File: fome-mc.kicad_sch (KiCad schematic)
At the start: 3 parts, among them J1 TE_776163-1, J2 TE_776163-2

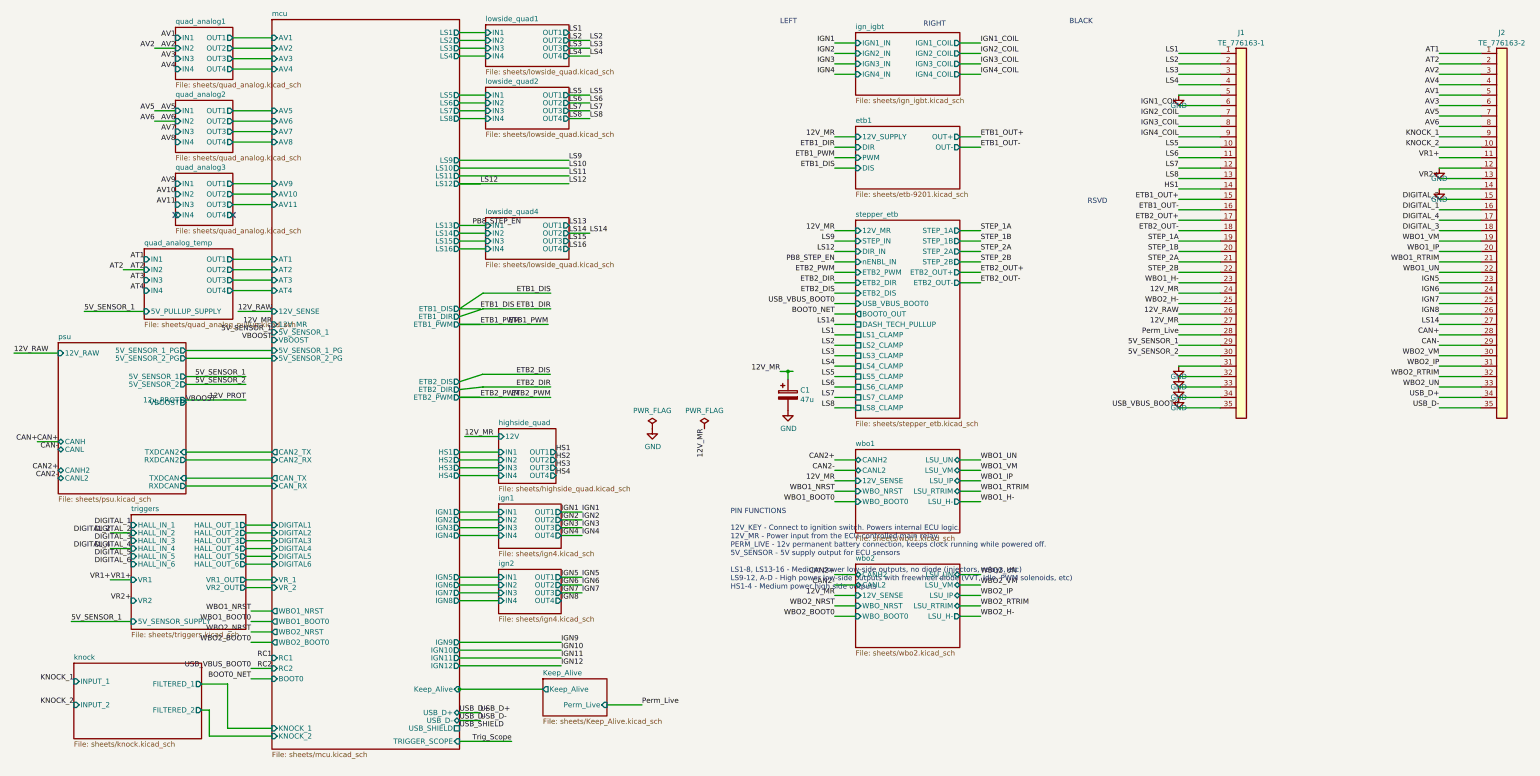
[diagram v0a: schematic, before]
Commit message: Remediate power supply, main relay keep-alive, and schematic ERC to 0 errors
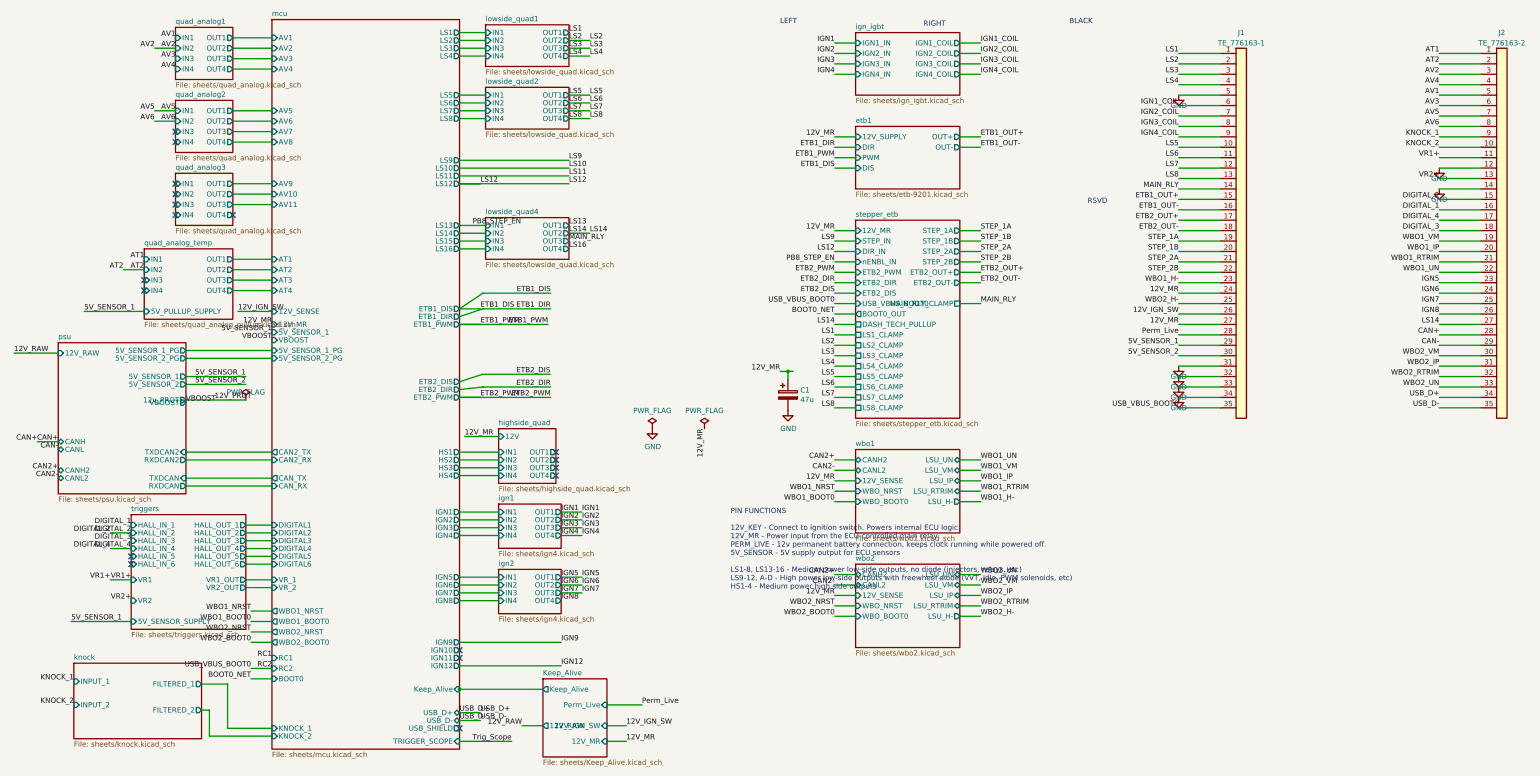
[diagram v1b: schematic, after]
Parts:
- C1: PN EEH-AZF1H560B -> EEHZC1H470P
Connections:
- net 12V_RAW: no longer J1.26 (Pin_26)
- net HS1 renamed MAIN_RLY
- new net 12V_IGN_SW: J1.26 (Pin_26)
- no-connect marks 2 -> 18
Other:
- sheet Keep_Alive ports: added 12V_IGN_SW, 12V_MR, 12V_RAW; removed none
- sheet stepper_etb ports: added MAIN_RLY_CLAMP; removed none

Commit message: Re-integrate ATWINC1500-MR210UB Wi-Fi on SPI4 and remap WBO1/2 reset/boot pins (FOMEMC-2)
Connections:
- no-connect marks 18 -> 16
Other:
- sheet mcu ports: added none; removed IGN10, IGN11, IGN12, IGN9
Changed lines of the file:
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@@
 	(wire
 		(pts
-			(xy 114.3 168.91) (xy 139.065 168.91)
-		)
-		(stroke
-			(width 0)
-			(type default)
-		)
-	)
-	(wire
-		(pts
 			(xy 194.31 102.87) (xy 195.58 102.87)
 		)
@@
 	(wire
 		(pts
-			(xy 114.3 174.625) (xy 139.065 174.625)
-		)
-		(stroke
-			(width 0)
-			(type default)
-		)
-	)
-	(wire
-		(pts
 			(xy 120.65 73.025) (xy 114.3 73.025)
 		)
@@
 		)
 	)
-	(label "IGN9"
-		(at 139.065 168.91 0)
-		(fields_autoplaced yes)
-		(effects
-			(font
-				(size 1.27 1.27)
-			)
-			(justify left bottom)
-		)
-	)
 	(label "LS12"
 		(at 140.97 57.15 0)
@@
 		)
 	)
-	(label "IGN12"
-		(at 139.065 174.625 0)
-		(fields_autoplaced yes)
-		(effects
-			(font
-				(size 1.27 1.27)
-			)
-			(justify left bottom)
-		)
-	)
 	(label "5V_SENSOR_1"
 		(at 22.86 88.265 0)
@@
 			)
 		)
-		(pin "IGN9" output
-			(at 114.3 168.91 0)
-			(effects
-				(font
-					(size 1.27 1.27)
-				)
-				(justify right)
-			)
-		)
-		(pin "IGN10" output
-			(at 114.3 170.815 0)
-			(effects
-				(font
-					(size 1.27 1.27)
-				)
-				(justify right)
-			)
-		)
-		(pin "IGN11" output
-			(at 114.3 172.72 0)
-			(effects
-				(font
-					(size 1.27 1.27)
-				)
-				(justify right)
-			)
-		)
-		(pin "IGN12" output
-			(at 114.3 174.625 0)
-			(effects
-				(font
-					(size 1.27 1.27)
-				)
-				(justify right)
-			)
-		)
 		(pin "USB_D-" bidirectional
 			(at 114.3 187.96 0)
@@
 		(at 137.795 128.27)
 	)
-	(no_connect
-		(at 114.3 170.815)
-	)
-	(no_connect
-		(at 114.3 172.72)
-	)
 )

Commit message: Add MAX9924UAUB+ (U13/U14) differential VR conditioners and switch Hall Schmitt triggers (U8/U9/U10) to +3V3 (FOMEMC-6)
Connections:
- net GND: no longer J2.12 (Pin_12), J2.14 (Pin_14)
- new net VR1-: J2.12 (Pin_12)
- new net VR2-: J2.14 (Pin_14)
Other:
- sheet triggers ports: added VR1-, VR2-; removed none
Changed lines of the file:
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@@
 		)
 	)
-	(label "VR1+"
-		(at 34.29 153.67 180)
+	(label "VR1-"
+		(at 34.29 156.21 180)
+		(fields_autoplaced yes)
+		(effects
+			(font
+				(size 1.27 1.27)
+			)
+			(justify right bottom)
+		)
+	)
+	(label "VR2-"
+		(at 34.29 161.29 180)
 		(fields_autoplaced yes)
 		(effects
@@
 			)
 		)
+		(pin "VR1-" input
+			(at 34.29 156.21 180)
+			(effects
+				(font
+					(size 1.27 1.27)
+				)
+				(justify left)
+			)
+		)
+		(pin "VR2-" input
+			(at 34.29 161.29 180)
+			(effects
+				(font
+					(size 1.27 1.27)
+				)
+				(justify left)
+			)
+		)
 		(pin "VR1_OUT" output
 			(at 62.23 153.67 0)
@@
 		)
 	)
-	(symbol
-		(lib_id "power:GND")
-		(at 353.06 53.34 0)
-		(unit 1)
-		(exclude_from_sim no)
-		(in_bom yes)
-		(on_board yes)
-		(dnp no)
-		(property "Reference" "#PWR07212" (at 353.06 55.88 0) (effects (font (size 1.27 1.27)) (hide yes)))
-		(property "Value" "GND" (at 353.06 55.88 0) (effects (font (size 1.27 1.27))))
-		(property "Footprint" "" (at 353.06 53.34 0) (effects (font (size 1.27 1.27)) (hide yes)))
-		(property "Datasheet" "" (at 353.06 53.34 0) (effects (font (size 1.27 1.27)) (hide yes)))
-		(pin "1")
-		(instances
-			(project "fome-mc" (path "/3b9c5ffd-e59b-402d-8c5e-052f7ca643a4" (reference "#PWR07212") (unit 1)))
-			(project "fome-mc" (path "/3b9c5ffd-e59b-402d-8c5e-052f7ca643a4" (reference "#PWR07212") (unit 1)))
+	(label "VR1-"
+		(at 353.06 53.34 180)
+		(fields_autoplaced yes)
+		(effects
+			(font
+				(size 1.27 1.27)
+			)
+			(justify right bottom)
 		)
 	)
@@
 		)
 	)
-	(symbol
-		(lib_id "power:GND")
-		(at 353.06 58.42 0)
-		(unit 1)
-		(exclude_from_sim no)
-		(in_bom yes)
-		(on_board yes)
-		(dnp no)
-		(property "Reference" "#PWR07214" (at 353.06 60.96 0) (effects (font (size 1.27 1.27)) (hide yes)))
-		(property "Value" "GND" (at 353.06 60.96 0) (effects (font (size 1.27 1.27))))
-		(property "Footprint" "" (at 353.06 58.42 0) (effects (font (size 1.27 1.27)) (hide yes)))
-		(property "Datasheet" "" (at 353.06 58.42 0) (effects (font (size 1.27 1.27)) (hide yes)))
-		(pin "1")
-		(instances
-			(project "fome-mc" (path "/3b9c5ffd-e59b-402d-8c5e-052f7ca643a4" (reference "#PWR07214") (unit 1)))
-			(project "fome-mc" (path "/3b9c5ffd-e59b-402d-8c5e-052f7ca643a4" (reference "#PWR07214") (unit 1)))
+	(label "VR2-"
+		(at 353.06 58.42 180)
+		(fields_autoplaced yes)
+		(effects
+			(font
+				(size 1.27 1.27)
+			)
+			(justify right bottom)
 		)
 	)

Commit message: Add D210 BZT52C6V8 BOOT0 threshold Zener, R217/R218/D211 PA9 VBUS sense divider/clamp, and SMCJ24A TVS protection on 12V_RAW and 12V_MR (FOMEMC-7)
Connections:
- net RC2: no longer J1.35 (Pin_35)
- new net USB_VBUS_BOOT0: J1.35 (Pin_35)
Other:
- sheet stepper_etb ports: added VBUS_SENSE_OUT; removed none
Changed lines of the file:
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@@
 			(effects (font (size 1.27 1.27)) (justify right))
 		)
+		(pin "VBUS_SENSE_OUT" output
+			(at 236.22 88.9 0)
+			(effects (font (size 1.27 1.27)) (justify right))
+		)
 		(instances
-			(project "fome-mc" (path "/3b9c5ffd-e59b-402d-8c5e-052f7ca643a4" (page "19")))
 			(project "fome-mc" (path "/3b9c5ffd-e59b-402d-8c5e-052f7ca643a4" (page "19")))
 		)
@@
 	(wire
 		(pts
-			(xy 63.5 175.26) (xy 68.58 175.26)
-		)
-		(stroke
-			(width 0)
-			(type default)
-		)
-	)
-	(label "USB_VBUS_BOOT0"
-		(at 63.5 175.26 180)
-		(fields_autoplaced yes)
-		(effects
-			(font
-				(size 1.27 1.27)
-			)
-			(justify right bottom)
-		)
-	)
+			(xy 236.22 88.9) (xy 241.3 88.9)
+		)
+		(stroke
+			(width 0)
+			(type default)
+		)
+	)
+	(label "RC2"
+		(at 241.3 88.9 0)
+		(fields_autoplaced yes)
+		(effects
+			(font
+				(size 1.27 1.27)
+			)
+			(justify left bottom)
+		)
+	)

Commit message: Complete FOMEMC-11, FOMEMC-12, and FOMEMC-16: sync 492 PCB footprints, restore min_resolved_spokes=2 (0 starved thermals), enable teardrops, enforce >=1.2mm IGBT collector clearance, widen /IGN1..4_COIL, add WBO heater copper zones, and refresh CPL/BOM/renders
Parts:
- added R219: 1.5k, Resistor_SMD:R_0603_1608Metric, symbol Device:R
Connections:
- net 5V_SENSOR_1: now also R219.1
- net AV6: now also R219.2
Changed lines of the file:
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@@
 		(color 0 0 0 0)
 	)
-	(junction
-		(at 114.3 180.34)
-		(diameter 0)
-		(color 0 0 0 0)
-	)
 	(no_connect
 		(at 45.085 64.77)
@@
 	(wire
 		(pts
-			(xy 194.31 102.87) (xy 195.58 102.87)
-		)
-		(stroke
-			(width 0)
-			(type default)
-		)
-	)
-	(wire
-		(pts
 			(xy 62.23 106.045) (xy 47.625 106.045)
 		)
@@
 	(wire
 		(pts
-			(xy 114.3 180.325) (xy 114.3 180.34)
-		)
-		(stroke
-			(width 0)
-			(type default)
-		)
-	)
-	(wire
-		(pts
 			(xy 120.65 41.275) (xy 114.3 41.275)
 		)
@@
 		)
 	)
-	(wire
-		(pts
-			(xy 194.31 102.87) (xy 194.343 102.899)
-		)
-		(stroke
-			(width 0)
-			(type default)
-		)
-	)
 	(text "LEFT"
 		(exclude_from_sim no)
@@
 	(wire
 		(pts
-			(xy 114.3 87.63) (xy 119.38 87.63)
-		)
-		(stroke
-			(width 0)
-			(type default)
-		)
-	)
-	(label "ETB1_DIS"
-		(at 119.38 87.63 0)
-		(fields_autoplaced yes)
-		(effects
-			(font
-				(size 1.27 1.27)
-			)
-			(justify left bottom)
-		)
-	)
-	(wire
-		(pts
 			(xy 114.3 91.44) (xy 119.38 91.44)
 		)
@@
 		)
 	)
-	(label "LS14"
+	(label "LS8"
 		(at 205.74 91.44 180)
 		(fields_autoplaced yes)
@@
 		(at 137.795 128.27)
 	)
+	(wire
+		(pts
+			(xy 19.05 41.91) (xy 21.59 41.91)
+		)
+		(stroke (width 0) (type default))
+	)
+	(label "5V_SENSOR_1"
+		(at 19.05 41.91 180)
+		(fields_autoplaced yes)
+		(effects (font (size 1.27 1.27)) (justify right bottom))
+	)
+	(wire
+		(pts
+			(xy 29.21 41.91) (xy 34.29 41.91)
+		)
+		(stroke (width 0) (type default))
+	)
+	(label "AV6"
+		(at 34.29 41.91 0)
+		(fields_autoplaced yes)
+		(effects (font (size 1.27 1.27)) (justify left bottom))
+	)
+	(symbol
+		(lib_id "Device:R")
+		(at 25.4 41.91 90)
+		(unit 1)
+		(exclude_from_sim no)
+		(in_bom yes)
+		(on_board yes)
+		(dnp no)
+		(fields_autoplaced yes)
+		(property "Reference" "R219"
+			(at 25.4 39.37 0)
+			(effects (font (size 1.27 1.27)))
+		)
+		(property "Value" "1.5k"
+			(at 25.4 44.45 0)
+			(effects (font (size 1.27 1.27)))
+		)
+		(property "Footprint" "Resistor_SMD:R_0603_1608Metric"
+			(at 25.4 41.91 0)
+			(effects (font (size 1.27 1.27)) (hide yes))
+		)
+		(property "Datasheet" "~"
+			(at 25.4 41.91 0)
+			(effects (font (size 1.27 1.27)) (hide yes))
+		)
+		(property "Description" "1.5kOhm 1% 0603 Thick Film Resistor (Gear Position Pull-Up)"
+			(at 25.4 41.91 0)
+			(effects (font (size 1.27 1.27)) (hide yes))
+		)
+		(property "PN" "0603WAF1501T5E"
+			(at 25.4 41.91 0)
+			(effects (font (size 1.27 1.27)) (hide yes))
+		)
+		(property "LCSC" "C22843"
+			(at 25.4 41.91 0)
+			(effects (font (size 1.27 1.27)) (hide yes))
+		)
+		(pin "1")
+		(pin "2")
+		(instances
+			(project "fome-mc"
+				(path "/3b9c5ffd-e59b-402d-8c5e-052f7ca643a4"
+					(reference "R219")
+					(unit 1)
+				)
+			)
+		)
+	)
 )

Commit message: Remediate FOMEMC-17..20: 50V X7R PSU caps & 42V INJ clamp DNP, U29 DS70005304F footprint + 1P3V bypass, HV_IGN 0.50mm clearance + U25 decoupling, and 0 ERC violations
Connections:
- no-connect marks 16 -> 18
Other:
- sheet mcu ports: added none; removed LS10, LS11, RC1, TRIGGER_SCOPE
- sheet psu ports: added 12V_PROT; removed 12v_PROT
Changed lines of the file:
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@@
 	(wire
 		(pts
-			(xy 114.3 53.34) (xy 140.97 53.34)
-		)
-		(stroke
-			(width 0)
-			(type default)
-		)
-	)
-	(wire
-		(pts
 			(xy 120.015 106.68) (xy 114.3 107.315)
 		)
@@
 	(wire
 		(pts
-			(xy 114.3 55.245) (xy 140.97 55.245)
-		)
-		(stroke
-			(width 0)
-			(type default)
-		)
-	)
-	(wire
-		(pts
 			(xy 68.58 130.81) (xy 47.625 130.81)
 		)
@@
 	(wire
 		(pts
-			(xy 114.3 193.04) (xy 127 193.04)
-		)
-		(stroke
-			(width 0)
-			(type default)
-		)
-	)
-	(wire
-		(pts
 			(xy 114.3 139.065) (xy 123.825 139.065)
 		)
@@
 		)
 	)
-	(label "LS16"
-		(at 140.97 73.025 0)
-		(fields_autoplaced yes)
-		(effects
-			(font
-				(size 1.27 1.27)
-			)
-			(justify left bottom)
-		)
-	)
 	(label "12V_RAW"
 		(at 5.715 98.425 0)
@@
 		)
 	)
-	(label "Trig_Scope"
-		(at 127 193.04 180)
-		(fields_autoplaced yes)
-		(effects
-			(font
-				(size 1.27 1.27)
-			)
-			(justify right bottom)
-		)
-	)
 	(label "LS1"
 		(at 140.97 20.32 0)
@@
 		)
 	)
-	(label "LS10"
-		(at 140.97 53.34 0)
-		(fields_autoplaced yes)
-		(effects
-			(font
-				(size 1.27 1.27)
-			)
-			(justify left bottom)
-		)
-	)
 	(label "CAN-"
 		(at 16.51 121.92 180)
@@
 		)
 	)
-	(label "RC1"
-		(at 68.58 172.72 180)
-		(fields_autoplaced yes)
-		(effects
-			(font
-				(size 1.27 1.27)
-			)
-			(justify right bottom)
-		)
-	)
 	(label "LS9"
 		(at 140.97 51.435 0)
@@
 		)
 	)
-	(label "LS13"
-		(at 140.97 67.31 0)
-		(fields_autoplaced yes)
-		(effects
-			(font
-				(size 1.27 1.27)
-			)
-			(justify left bottom)
-		)
-	)
 	(label "IGN4"
 		(at 139.065 142.875 0)
@@
 		)
 	)
-	(label "LS11"
-		(at 140.97 55.245 0)
-		(fields_autoplaced yes)
-		(effects
-			(font
-				(size 1.27 1.27)
-			)
-			(justify left bottom)
-		)
-	)
 	(label "KNOCK_1"
 		(at 20.32 178.435 180)
@@
 			)
 		)
-		(pin "LS10" output
-			(at 114.3 53.34 0)
-			(effects
-				(font
-					(size 1.27 1.27)
-				)
-				(justify right)
-			)
-		)
-		(pin "LS11" output
-			(at 114.3 55.245 0)
-			(effects
-				(font
-					(size 1.27 1.27)
-				)
-				(justify right)
-			)
-		)
 		(pin "LS13" output
 			(at 114.3 67.31 0)
@@
 			)
 		)
-		(pin "RC1" input
-			(at 68.58 172.72 180)
-			(effects
-				(font
-					(size 1.27 1.27)
-				)
-				(justify left)
-			)
-		)
 		(pin "RC2" input
 			(at 68.58 175.26 180)
@@
 			(effects (font (size 1.27 1.27)) (justify left))
 		)
-		(pin "TRIGGER_SCOPE" input
-			(at 114.3 193.04 0)
-			(effects
-				(font
-					(size 1.27 1.27)
-				)
-				(justify right)
-			)
-		)
 		(instances
 			(project "fome-mc"
@@
 			)
 		)
-		(pin "12v_PROT" output
+		(pin "12V_PROT" output
 			(at 47.625 109.855 0)
 			(effects
@@
 		(instances
 			(project "fome-mc" (path "/3b9c5ffd-e59b-402d-8c5e-052f7ca643a4" (page "17")))
-			(project "fome-mc" (path "/3b9c5ffd-e59b-402d-8c5e-052f7ca643a4" (page "17")))
 		)
 	)
@@
 		(instances
 			(project "fome-mc" (path "/3b9c5ffd-e59b-402d-8c5e-052f7ca643a4" (page "18")))
-			(project "fome-mc" (path "/3b9c5ffd-e59b-402d-8c5e-052f7ca643a4" (page "18")))
 		)
 	)
@@
 		(instances
 			(project "fome-mc" (path "/3b9c5ffd-e59b-402d-8c5e-052f7ca643a4" (page "20")))
-			(project "fome-mc" (path "/3b9c5ffd-e59b-402d-8c5e-052f7ca643a4" (page "20")))
 		)
 	)
@@
 		(instances
 			(project "fome-mc" (path "/3b9c5ffd-e59b-402d-8c5e-052f7ca643a4" (page "21")))
-			(project "fome-mc" (path "/3b9c5ffd-e59b-402d-8c5e-052f7ca643a4" (page "21")))
 		)
 	)
@@
 		(instances
 			(project "fome-mc" (path "/3b9c5ffd-e59b-402d-8c5e-052f7ca643a4" (reference "J1") (unit 1)))
-			(project "fome-mc" (path "/3b9c5ffd-e59b-402d-8c5e-052f7ca643a4" (reference "J1") (unit 1)))
 		)
 	)
@@
 		(instances
 			(project "fome-mc" (path "/3b9c5ffd-e59b-402d-8c5e-052f7ca643a4" (reference "#PWR07105") (unit 1)))
-			(project "fome-mc" (path "/3b9c5ffd-e59b-402d-8c5e-052f7ca643a4" (reference "#PWR07105") (unit 1)))
 		)
 	)
@@
 		(instances
 			(project "fome-mc" (path "/3b9c5ffd-e59b-402d-8c5e-052f7ca643a4" (reference "#PWR07131") (unit 1)))
-			(project "fome-mc" (path "/3b9c5ffd-e59b-402d-8c5e-052f7ca643a4" (reference "#PWR07131") (unit 1)))
 		)
 	)
@@
 		(instances
 			(project "fome-mc" (path "/3b9c5ffd-e59b-402d-8c5e-052f7ca643a4" (reference "#PWR07132") (unit 1)))
-			(project "fome-mc" (path "/3b9c5ffd-e59b-402d-8c5e-052f7ca643a4" (reference "#PWR07132") (unit 1)))
 		)
 	)
@@
 		(instances
 			(project "fome-mc" (path "/3b9c5ffd-e59b-402d-8c5e-052f7ca643a4" (reference "#PWR07133") (unit 1)))
-			(project "fome-mc" (path "/3b9c5ffd-e59b-402d-8c5e-052f7ca643a4" (reference "#PWR07133") (unit 1)))
 		)
 	)
@@
 		(instances
 			(project "fome-mc" (path "/3b9c5ffd-e59b-402d-8c5e-052f7ca643a4" (reference "#PWR07134") (unit 1)))
-			(project "fome-mc" (path "/3b9c5ffd-e59b-402d-8c5e-052f7ca643a4" (reference "#PWR07134") (unit 1)))
 		)
 	)
@@
 		(instances
 			(project "fome-mc" (path "/3b9c5ffd-e59b-402d-8c5e-052f7ca643a4" (reference "J2") (unit 1)))
-			(project "fome-mc" (path "/3b9c5ffd-e59b-402d-8c5e-052f7ca643a4" (reference "J2") (unit 1)))
 		)
 	)
@@
 		)
 	)
+	(no_connect
+		(at 140.97 67.31)
+	)
+	(no_connect
+		(at 140.97 73.025)
+	)
 	(sheet_instances
